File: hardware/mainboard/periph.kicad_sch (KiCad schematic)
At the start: 81 parts, among them J1 Micro_SD_Card_Det, P1 M2_SOCKET_E, Q1 BSS138, Q2 BSS138, Q3 BSS138, Q4 BSS138, Q5 BSS138, Q6 BSS138, Q7 BSS138, Q8 BSS138, SW2 SW_Push, SW3 SW_Push, SW4 SW_Push, SW5 SW_Push, SW6 SW_Push, U10 MMC5883MA, U11 Si52112-B, U21 74LVC2T45DC, U8 TXS02612, U9 ICM-20789, Y1 25MHz

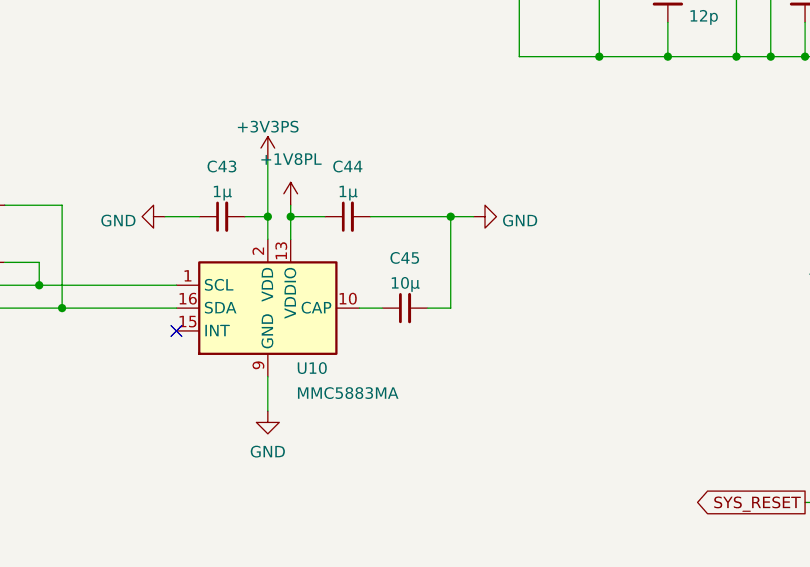
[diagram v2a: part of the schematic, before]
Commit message: Add some footprint mappings
Signed-off-by: gatecat <gatecat@ds0.me>
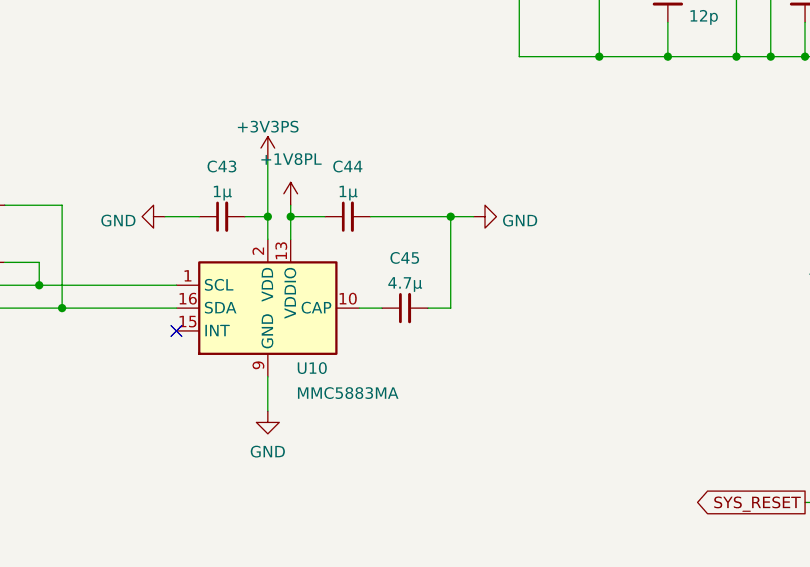
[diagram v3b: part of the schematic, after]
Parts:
- C41, C42: footprint Capacitor_SMD:C_0805_2012Metric -> Capacitor_SMD:C_1206_3216Metric
- C43, C44, C46, C47: footprint (none) -> Capacitor_SMD:C_0603_1608Metric
- C45: value 10µ -> 4.7µ; footprint (none) -> Capacitor_SMD:C_0603_1608Metric
- C48, C49, C50, C51, C52, C53: footprint (none) -> Capacitor_SMD:C_0402_1005Metric
- FB2: footprint (none) -> Inductor_SMD:L_0603_1608Metric
- P1: footprint (none) -> meowality:2199230-4
- R41, R42, R43, R44, R45, R46, R47: footprint (none) -> Resistor_SMD:R_0402_1005Metric
- SW2, SW3, SW4, SW5, SW6: footprint (none) -> Button_Switch_SMD:SW_SPST_B3S-1000
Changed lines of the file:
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@@
     (property "Reference" "SW2" (id 0) (at 252.73 182.88 0))
     (property "Value" "SW_Push" (id 1) (at 252.73 185.42 0))
-    (property "Footprint" "" (id 2) (at 252.73 185.42 0)
+    (property "Footprint" "Button_Switch_SMD:SW_SPST_B3S-1000" (id 2) (at 252.73 185.42 0)
       (effects (font (size 1.27 1.27)) hide)
     )
@@
     (property "Reference" "C53" (id 0) (at 308.61 140.97 90))
     (property "Value" "100n" (id 1) (at 316.23 140.97 90))
-    (property "Footprint" "" (id 2) (at 312.42 142.24 0)
+    (property "Footprint" "Capacitor_SMD:C_0402_1005Metric" (id 2) (at 312.42 142.24 0)
       (effects (font (size 1.27 1.27)) hide)
     )
@@
       (effects (font (size 1.27 1.27)) (justify left))
     )
-    (property "Footprint" "Capacitor_SMD:C_0805_2012Metric" (id 2) (at 140.97 27.94 0)
+    (property "Footprint" "Capacitor_SMD:C_1206_3216Metric" (id 2) (at 140.97 27.94 0)
       (effects (font (size 1.27 1.27)) hide)
     )
@@
     (property "Reference" "P1" (id 0) (at 363.22 59.6604 0))
     (property "Value" "M2_SOCKET_E" (id 1) (at 363.22 62.4355 0))
-    (property "Footprint" "" (id 2) (at 363.22 82.55 0)
+    (property "Footprint" "meowality:2199230-4" (id 2) (at 363.22 82.55 0)
       (effects (font (size 1.27 1.27)) hide)
     )
@@
     (property "Reference" "SW3" (id 0) (at 271.78 218.44 0))
     (property "Value" "SW_Push" (id 1) (at 271.78 220.98 0))
-    (property "Footprint" "" (id 2) (at 271.78 220.98 0)
+    (property "Footprint" "Button_Switch_SMD:SW_SPST_B3S-1000" (id 2) (at 271.78 220.98 0)
       (effects (font (size 1.27 1.27)) hide)
     )
@@
     (property "Reference" "SW5" (id 0) (at 271.78 238.76 0))
     (property "Value" "SW_Push" (id 1) (at 271.78 241.3 0))
-    (property "Footprint" "" (id 2) (at 271.78 241.3 0)
+    (property "Footprint" "Button_Switch_SMD:SW_SPST_B3S-1000" (id 2) (at 271.78 241.3 0)
       (effects (font (size 1.27 1.27)) hide)
     )
@@
     (property "Reference" "R46" (id 0) (at 287.02 112.1369 90))
     (property "Value" "0R" (id 1) (at 312.42 114.912 90))
-    (property "Footprint" "" (id 2) (at 312.42 116.84 0)
+    (property "Footprint" "Resistor_SMD:R_0402_1005Metric" (id 2) (at 312.42 116.84 0)
       (effects (font (size 1.27 1.27)) hide)
     )
@@
     (property "Reference" "FB2" (id 0) (at 204.47 103.5517 90))
     (property "Value" "Ferrite_Bead_Small" (id 1) (at 204.47 106.3268 90))
-    (property "Footprint" "" (id 2) (at 204.47 110.998 90)
+    (property "Footprint" "Inductor_SMD:L_0603_1608Metric" (id 2) (at 204.47 110.998 90)
       (effects (font (size 1.27 1.27)) hide)
     )
@@
     (property "Reference" "C50" (id 0) (at 308.61 107.95 90))
     (property "Value" "100n" (id 1) (at 316.23 107.95 90))
-    (property "Footprint" "" (id 2) (at 312.42 109.22 0)
+    (property "Footprint" "Capacitor_SMD:C_0402_1005Metric" (id 2) (at 312.42 109.22 0)
       (effects (font (size 1.27 1.27)) hide)
     )
@@
     (property "Reference" "C52" (id 0) (at 308.61 138.43 90))
     (property "Value" "100n" (id 1) (at 316.23 138.43 90))
-    (property "Footprint" "" (id 2) (at 312.42 139.7 0)
+    (property "Footprint" "Capacitor_SMD:C_0402_1005Metric" (id 2) (at 312.42 139.7 0)
       (effects (font (size 1.27 1.27)) hide)
     )
@@
     (in_bom yes) (on_board yes)
     (property "Reference" "C45" (id 0) (at 196.85 163.3814 90))
-    (property "Value" "10µ" (id 1) (at 196.85 166.1565 90))
-    (property "Footprint" "" (id 2) (at 196.85 168.91 0)
+    (property "Value" "4.7µ" (id 1) (at 196.85 166.1565 90))
+    (property "Footprint" "Capacitor_SMD:C_0603_1608Metric" (id 2) (at 196.85 168.91 0)
       (effects (font (size 1.27 1.27)) hide)
     )
@@
       (effects (font (size 1.27 1.27)) (justify left))
     )
-    (property "Footprint" "" (id 2) (at 226.06 134.62 0)
+    (property "Footprint" "Capacitor_SMD:C_0402_1005Metric" (id 2) (at 226.06 134.62 0)
       (effects (font (size 1.27 1.27)) hide)
     )
@@
     (property "Reference" "SW6" (id 0) (at 271.78 248.92 0))
     (property "Value" "SW_Push" (id 1) (at 271.78 251.46 0))
-    (property "Footprint" "" (id 2) (at 271.78 251.46 0)
+    (property "Footprint" "Button_Switch_SMD:SW_SPST_B3S-1000" (id 2) (at 271.78 251.46 0)
       (effects (font (size 1.27 1.27)) hide)
     )
@@
     (property "Reference" "C43" (id 0) (at 176.53 153.2214 90))
     (property "Value" "1µ" (id 1) (at 176.53 155.9965 90))
-    (property "Footprint" "" (id 2) (at 176.53 158.75 0)
+    (property "Footprint" "Capacitor_SMD:C_0603_1608Metric" (id 2) (at 176.53 158.75 0)
       (effects (font (size 1.27 1.27)) hide)
     )
@@
     (property "Reference" "SW4" (id 0) (at 271.78 228.6 0))
     (property "Value" "SW_Push" (id 1) (at 271.78 231.14 0))
-    (property "Footprint" "" (id 2) (at 271.78 231.14 0)
+    (property "Footprint" "Button_Switch_SMD:SW_SPST_B3S-1000" (id 2) (at 271.78 231.14 0)
       (effects (font (size 1.27 1.27)) hide)
     )
@@
     (property "Reference" "R47" (id 0) (at 312.42 123.5669 90))
     (property "Value" "0R" (id 1) (at 312.42 121.262 90))
-    (property "Footprint" "" (id 2) (at 312.42 119.38 0)
+    (property "Footprint" "Resistor_SMD:R_0402_1005Metric" (id 2) (at 312.42 119.38 0)
       (effects (font (size 1.27 1.27)) hide)
     )
@@
       (effects (font (size 1.27 1.27)) (justify left))
     )
-    (property "Footprint" "" (id 2) (at 245.11 220.98 0)
+    (property "Footprint" "Resistor_SMD:R_0402_1005Metric" (id 2) (at 245.11 220.98 0)
       (effects (font (size 1.27 1.27)) hide)
     )
@@
       (effects (font (size 1.27 1.27)) (justify left))
     )
-    (property "Footprint" "" (id 2) (at 209.55 124.46 0)
+    (property "Footprint" "Capacitor_SMD:C_0603_1608Metric" (id 2) (at 209.55 124.46 0)
       (effects (font (size 1.27 1.27)) hide)
     )
@@
       (effects (font (size 1.27 1.27)) (justify left))
     )
-    (property "Footprint" "" (id 2) (at 241.3 134.62 0)
+    (property "Footprint" "Capacitor_SMD:C_0402_1005Metric" (id 2) (at 241.3 134.62 0)
       (effects (font (size 1.27 1.27)) hide)
     )
@@
       (effects (font (size 1.27 1.27)) (justify left))
     )
-    (property "Footprint" "" (id 2) (at 218.44 124.46 0)
+    (property "Footprint" "Capacitor_SMD:C_0603_1608Metric" (id 2) (at 218.44 124.46 0)
       (effects (font (size 1.27 1.27)) hide)
     )
@@
     (property "Reference" "C51" (id 0) (at 308.61 110.49 90))
     (property "Value" "100n" (id 1) (at 316.23 110.49 90))
-    (property "Footprint" "" (id 2) (at 312.42 111.76 0)
+    (property "Footprint" "Capacitor_SMD:C_0402_1005Metric" (id 2) (at 312.42 111.76 0)
       (effects (font (size 1.27 1.27)) hide)
     )
@@
       (effects (font (size 1.27 1.27)) (justify left))
     )
-    (property "Footprint" "" (id 2) (at 250.19 231.14 0)
+    (property "Footprint" "Resistor_SMD:R_0402_1005Metric" (id 2) (at 250.19 231.14 0)
       (effects (font (size 1.27 1.27)) hide)
     )
@@
     (property "Reference" "C44" (id 0) (at 190.5 153.2214 90))
     (property "Value" "1µ" (id 1) (at 190.5 155.9965 90))
-    (property "Footprint" "" (id 2) (at 190.5 158.75 0)
+    (property "Footprint" "Capacitor_SMD:C_0603_1608Metric" (id 2) (at 190.5 158.75 0)
       (effects (font (size 1.27 1.27)) hide)
     )
@@
       (effects (font (size 1.27 1.27)) (justify left))
     )
-    (property "Footprint" "" (id 2) (at 255.27 241.3 0)
+    (property "Footprint" "Resistor_SMD:R_0402_1005Metric" (id 2) (at 255.27 241.3 0)
       (effects (font (size 1.27 1.27)) hide)
     )
@@
       (effects (font (size 1.27 1.27)) (justify left))
     )
-    (property "Footprint" "Capacitor_SMD:C_0805_2012Metric" (id 2) (at 149.86 27.94 0)
+    (property "Footprint" "Capacitor_SMD:C_1206_3216Metric" (id 2) (at 149.86 27.94 0)
       (effects (font (size 1.27 1.27)) hide)
     )
@@
       (effects (font (size 1.27 1.27)) (justify left))
     )
-    (property "Footprint" "" (id 2) (at 245.11 177.8 0)
+    (property "Footprint" "Resistor_SMD:R_0402_1005Metric" (id 2) (at 245.11 177.8 0)
       (effects (font (size 1.27 1.27)) hide)
     )
@@
       (effects (font (size 1.27 1.27)) (justify left))
     )
-    (property "Footprint" "" (id 2) (at 260.35 251.46 0)
-      (effects (font (size 1.27 1.27)) hide)
-    )
+    (property "Footprint" "Resistor_SMD:R_0402_1005Metric" (id 2) (at 260.35 251.46 0)
+      (effects (font (size 1.27 1.27)) hide)
+    )

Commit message: Footprint assignments and related fixes
Signed-off-by: gatecat <gatecat@ds0.me>
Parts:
- U21: footprint Package_SO:VSSOP-8_2.3x2mm_P0.5mm -> Package_SON:X2SON-8_1.4x1mm_P0.35mm
- U9: footprint (none) -> Sensor_Motion:InvenSense_QFN-24_4x4mm_P0.5mm
- Y1: footprint (none) -> Crystal:Crystal_SMD_3225-4Pin_3.2x2.5mm
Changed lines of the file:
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@@
     (property "Reference" "U9" (id 0) (at 107.95 107.8443 0))
     (property "Value" "ICM-20789" (id 1) (at 107.95 110.6194 0))
-    (property "Footprint" "" (id 2) (at 107.95 154.94 0)
+    (property "Footprint" "Sensor_Motion:InvenSense_QFN-24_4x4mm_P0.5mm" (id 2) (at 107.95 154.94 0)
       (effects (font (size 1.27 1.27)) hide)
     )
@@
       (effects (font (size 1.27 1.27)) (justify left))
     )
-    (property "Footprint" "Package_SO:VSSOP-8_2.3x2mm_P0.5mm" (id 2) (at 323.85 232.41 0)
+    (property "Footprint" "Package_SON:X2SON-8_1.4x1mm_P0.35mm" (id 2) (at 323.85 232.41 0)
       (effects (font (size 1.27 1.27)) hide)
     )
@@
       (effects (font (size 1.27 1.27)) (justify left))
     )
-    (property "Footprint" "" (id 2) (at 233.68 129.54 0)
-      (effects (font (size 1.27 1.27)) hide)
-    )
+    (property "Footprint" "Crystal:Crystal_SMD_3225-4Pin_3.2x2.5mm" (id 2) (at 233.68 129.54 0)
+      (effects (font (size 1.27 1.27)) hide)
+    )

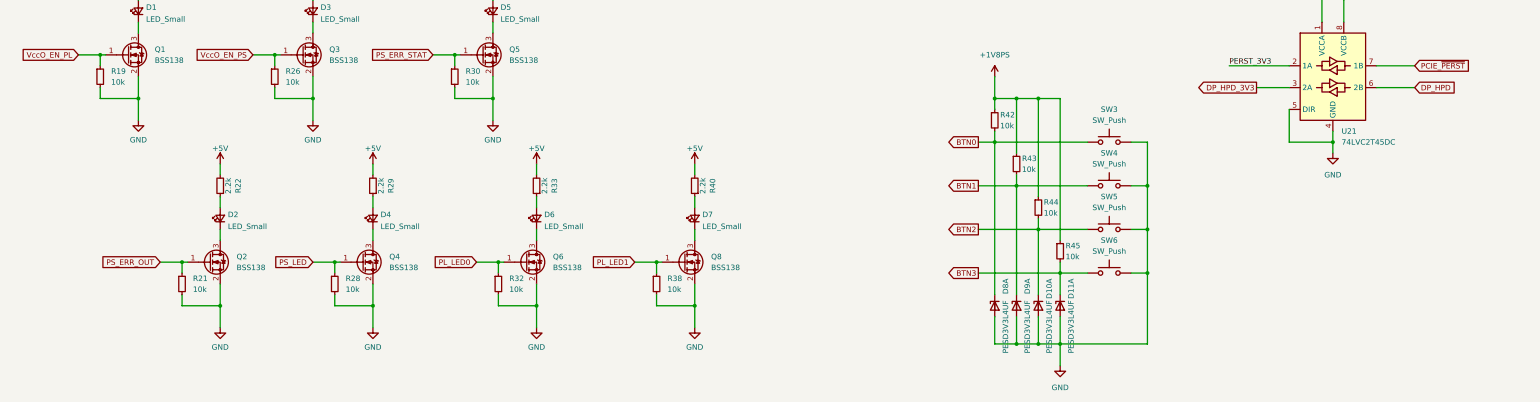
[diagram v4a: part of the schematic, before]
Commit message: Rework power arch to add 3V3PL; 5x PL RGB LEDs
Signed-off-by: gatecat <gatecat@ds0.me>
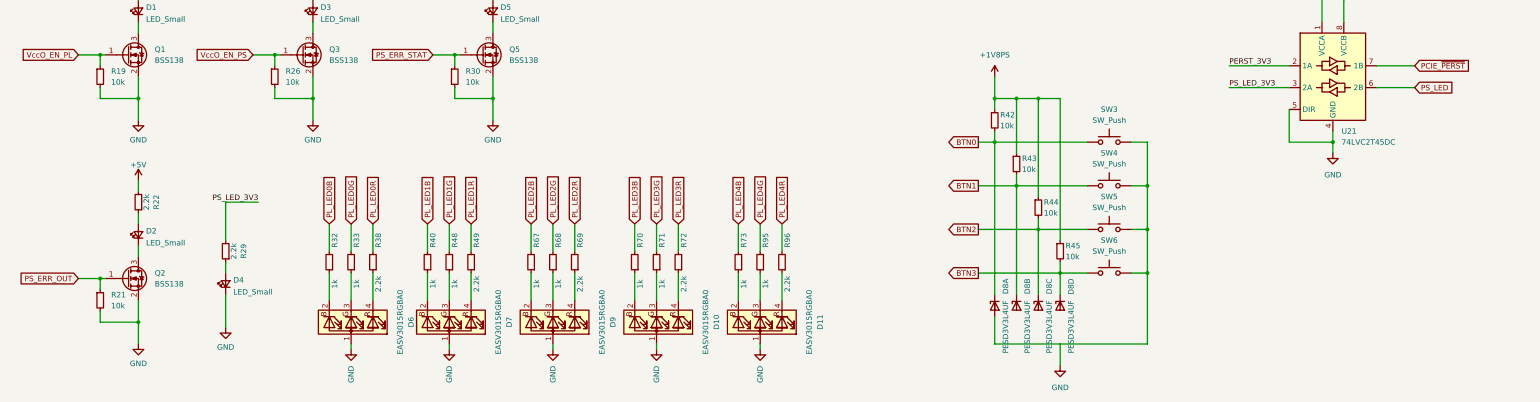
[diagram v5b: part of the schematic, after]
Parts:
- removed D6, D7: LED_Small, LED_SMD:LED_0603_1608Metric, symbol Device:LED_Small
- removed Q4, Q6, Q8: BSS138, Package_TO_SOT_SMD:SOT-23, symbol Transistor_FET:BSS138
- removed R28: 10k, Resistor_SMD:R_0402_1005Metric, symbol Device:R_Small
- added D10, D11, D6, D7, D9: EASV3015RGBA0, symbol Device:LED_ABGR
- added R48, R67, R68, R70, R71, R73, R95: 1k, Resistor_SMD:R_0402_1005Metric, symbol Device:R_Small
- added R49, R69, R72, R96: 2.2k, Resistor_SMD:R_0402_1005Metric, symbol Device:R_Small
- R32: value 10k -> 1k
- R33, R40: value 2.2k -> 1k
- R38: value 10k -> 2.2k
- renumbered D11 to D8, D9 to D8, D10 to D8
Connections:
- net DP_HPD is gone; now on net PS_LED: U21.6 (2B)
- net +5V: no longer R29.2, R33.2, R40.2
- net BTN1: now also D8.3 (K2); no longer D8.1 (K1)
- net BTN2: now also D8.4 (K3); no longer D8.1 (K1)
- net BTN3: now also D8.6 (K4); no longer D8.1 (K1)
- net GND: now also D4.1 (K), D10.1 (A), D11.1 (A), D6.1 (A), D7.1 (A), D9.1 (A); no longer D8.2 (A), D8.2 (A), D8.2 (A), D8.2 (A), D8.5 (A), D8.5 (A), D8.5 (A), D8.5 (A), R32.2, R38.2, SW3.2, SW4.2, SW5.2, SW6.2
- net at R40.1: now also D7.2 (BK)
- net at R33.1: now also D6.3 (GK)
- net DP_HPD_3V3 renamed PS_LED_3V3
- net PS_LED_3V3: now also R29.2
- net PL_LED0: no longer names the net of R32.1
- net PL_LED0: now also D6.2 (BK)
- net PL_LED1: no longer names the net of R38.1
- net PL_LED1: now also D6.4 (RK)
- new net: D10.3 (GK), R71.1
- new net: D8.2 (A), D8.5 (A), SW3.2, SW4.2, SW5.2, SW6.2
- new net: D7.4 (RK), R49.1
- new net: D10.2 (BK), R70.1
- new net: D10.4 (RK), R72.1
- new net: D9.2 (BK), R67.1
- new net: D7.3 (GK), R48.1
- new net: D11.2 (BK), R73.1
- new net: D11.3 (GK), R95.1
- new net: D11.4 (RK), R96.1
- new net: D9.3 (GK), R68.1
- new net: D9.4 (RK), R69.1
- new net PL_LED0B: R32.2
- new net PL_LED0G: R33.2
- new net PL_LED0R: R38.2
- new net PL_LED1B: R40.2
- new net PL_LED1G: R48.2
- new net PL_LED1R: R49.2
- new net PL_LED2B: R67.2
- new net PL_LED2G: R68.2
- new net PL_LED2R: R69.2
- new net PL_LED3B: R70.2
- new net PL_LED3G: R71.2
- new net PL_LED3R: R72.2
- new net PL_LED4B: R73.2
- new net PL_LED4G: R95.2
- new net PL_LED4R: R96.2
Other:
- moved on the sheet: D2, D4, Q2, R21, R22, R29

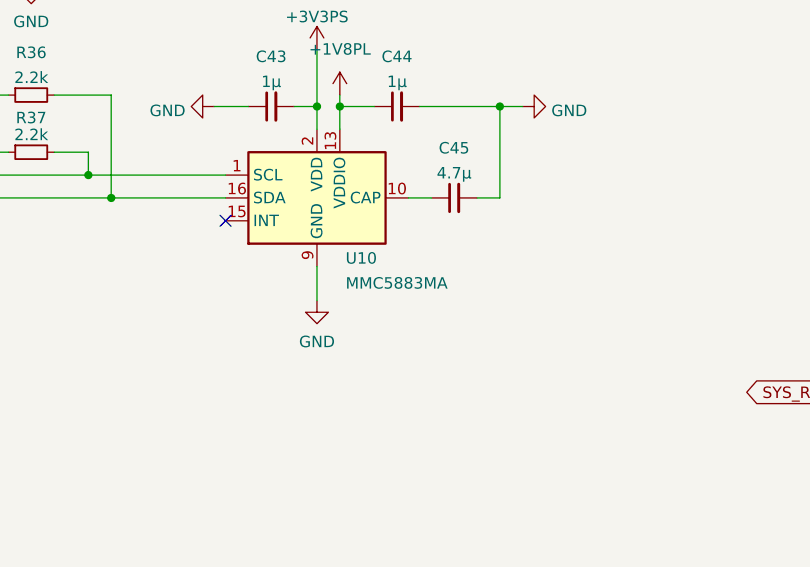
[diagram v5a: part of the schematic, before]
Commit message: Footprint assignment updates
Signed-off-by: gatecat <gatecat@ds0.me>
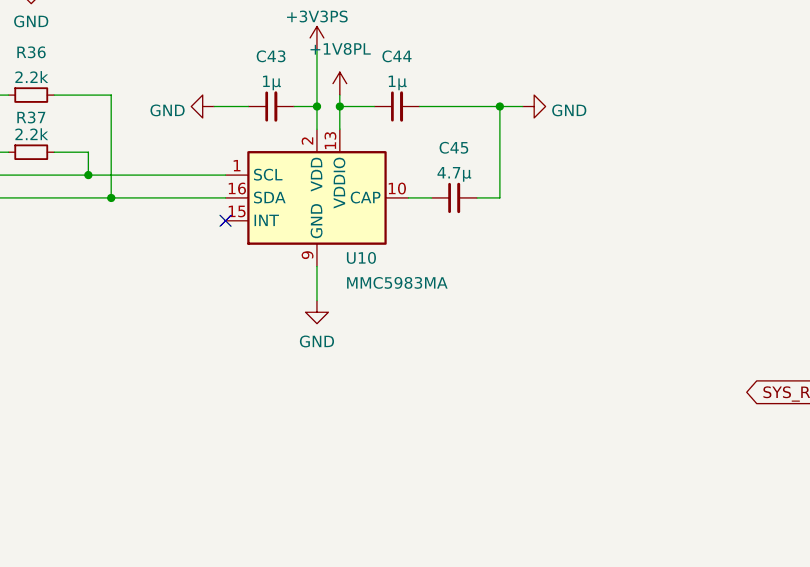
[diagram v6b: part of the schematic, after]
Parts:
- D10, D11, D6, D7, D9: footprint (none) -> meowality:EASV3015R
- U10: value MMC5883MA -> MMC5983MA
- U11: footprint (none) -> meowality:TDFN10_3x3mm_p0.5mm
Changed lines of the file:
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@@
       (effects (font (size 1.27 1.27)) (justify left))
     )
-    (property "Value" "MMC5883MA" (id 1) (at 184.7851 178.3966 0)
+    (property "Value" "MMC5983MA" (id 1) (at 184.7851 178.3966 0)
       (effects (font (size 1.27 1.27)) (justify left))
     )
@@
     (property "Reference" "D10" (id 0) (at 180.34 267.97 0))
     (property "Value" "EASV3015RGBA0" (id 1) (at 177.8 267.97 0))
-    (property "Footprint" "" (id 2) (at 165.1 267.97 0)
+    (property "Footprint" "meowality:EASV3015R" (id 2) (at 165.1 267.97 0)
       (effects (font (size 1.27 1.27)) hide)
     )
@@
     (property "Reference" "D7" (id 0) (at 132.08 267.97 0))
     (property "Value" "EASV3015RGBA0" (id 1) (at 129.54 267.97 0))
-    (property "Footprint" "" (id 2) (at 116.84 267.97 0)
+    (property "Footprint" "meowality:EASV3015R" (id 2) (at 116.84 267.97 0)
       (effects (font (size 1.27 1.27)) hide)
     )
@@
     (property "Reference" "D11" (id 0) (at 204.47 267.97 0))
     (property "Value" "EASV3015RGBA0" (id 1) (at 201.93 267.97 0))
-    (property "Footprint" "" (id 2) (at 189.23 267.97 0)
+    (property "Footprint" "meowality:EASV3015R" (id 2) (at 189.23 267.97 0)
       (effects (font (size 1.27 1.27)) hide)
     )
@@
     (property "Reference" "D9" (id 0) (at 156.21 267.97 0))
     (property "Value" "EASV3015RGBA0" (id 1) (at 153.67 267.97 0))
-    (property "Footprint" "" (id 2) (at 140.97 267.97 0)
+    (property "Footprint" "meowality:EASV3015R" (id 2) (at 140.97 267.97 0)
       (effects (font (size 1.27 1.27)) hide)
     )
@@
     (property "Reference" "D6" (id 0) (at 109.22 267.97 0))
     (property "Value" "EASV3015RGBA0" (id 1) (at 106.68 267.97 0))
-    (property "Footprint" "" (id 2) (at 93.98 267.97 0)
+    (property "Footprint" "meowality:EASV3015R" (id 2) (at 93.98 267.97 0)
       (effects (font (size 1.27 1.27)) hide)
     )
@@
     (property "Reference" "U11" (id 0) (at 270.51 107.92 0))
     (property "Value" "Si52112-B" (id 1) (at 270.51 110.6951 0))
-    (property "Footprint" "" (id 2) (at 270.51 139.7 0)
-      (effects (font (size 1.27 1.27)) hide)
-    )
+    (property "Footprint" "meowality:TDFN10_3x3mm_p0.5mm" (id 2) (at 270.51 139.7 0)
+      (effects (font (size 1.27 1.27)) hide)
+    )
